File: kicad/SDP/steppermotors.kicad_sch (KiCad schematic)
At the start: 54 parts, among them J17 Conn_01x04, J18 Conn_01x04, J19 Conn_01x04, J20 Conn_01x04, J21 Conn_01x04, J22 Conn_01x04

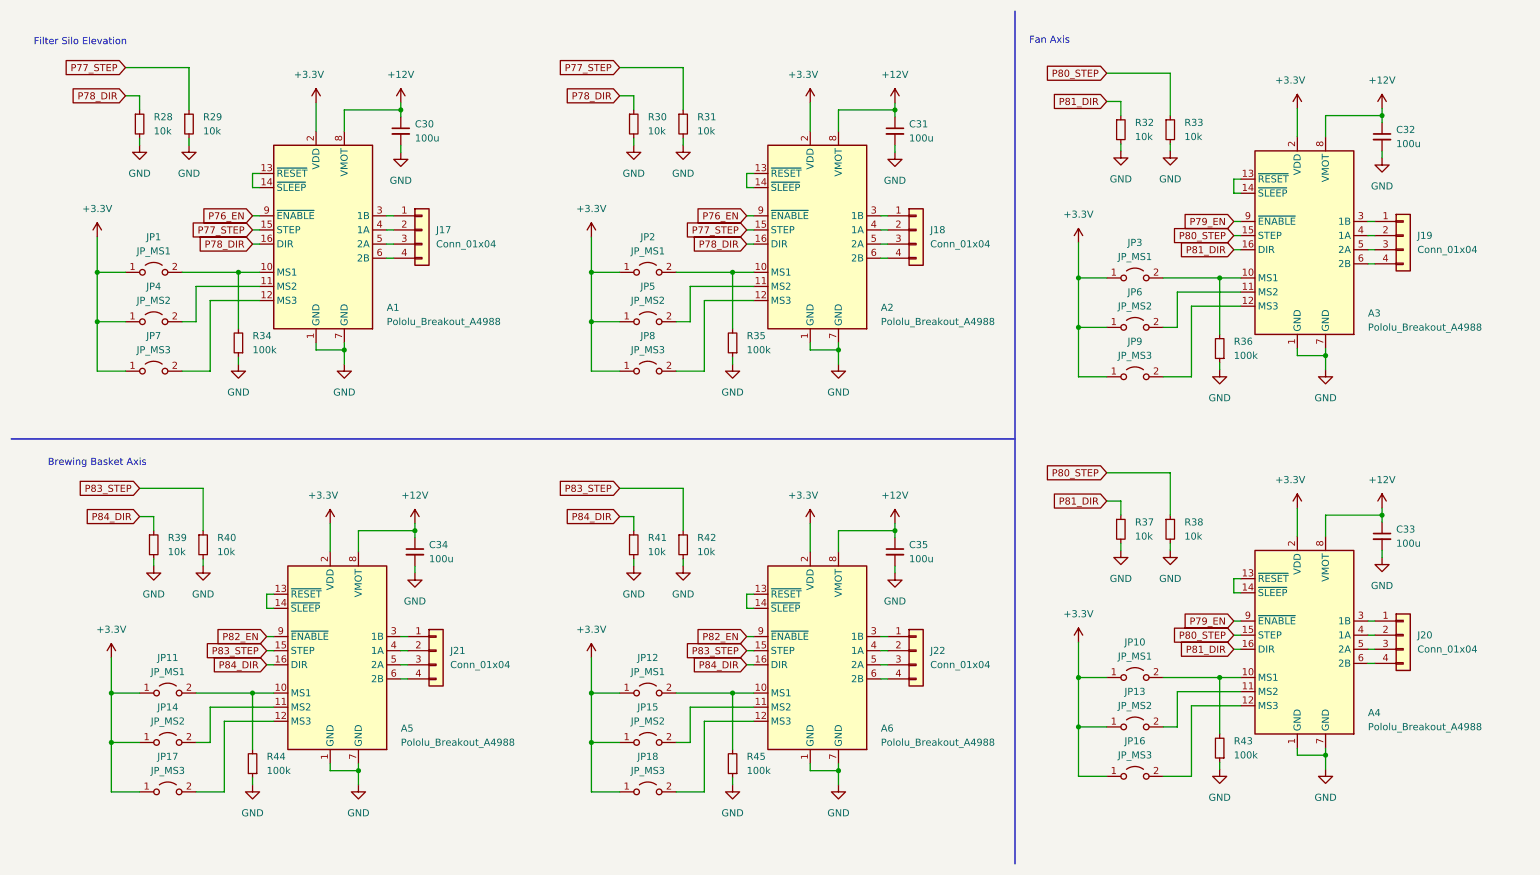
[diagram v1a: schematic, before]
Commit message: PCB layout and footprint assignment fix
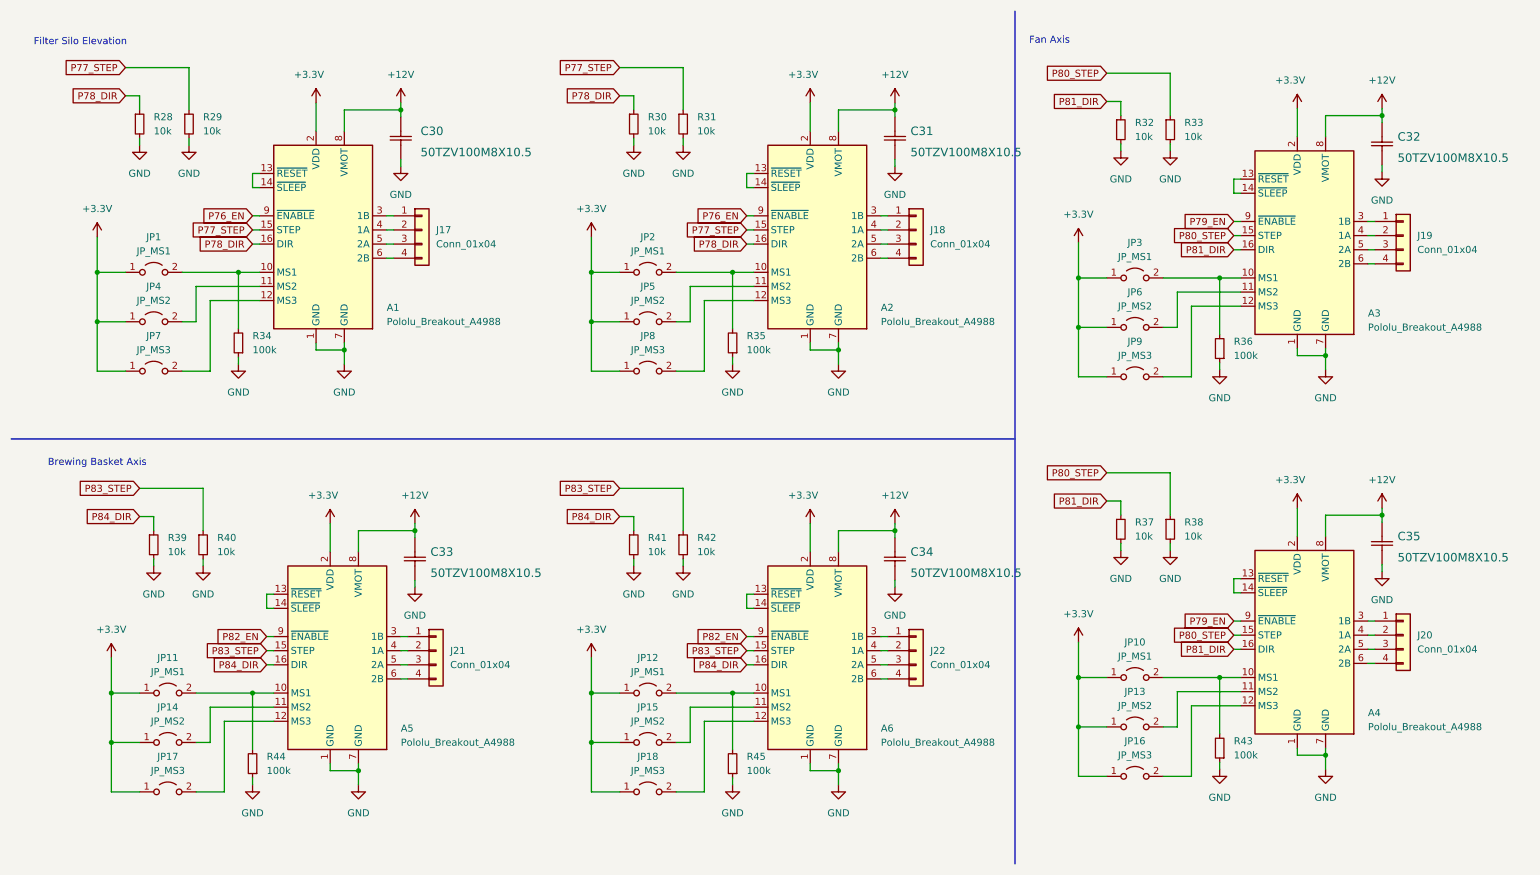
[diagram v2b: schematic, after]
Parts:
- removed C30, C31, C32, C33, C34, C35: 100u, footprints:50TZV100M8X10.5, symbol Device:C_Small
- added C30, C31, C32, C33, C34, C35: 50TZV100M8X10.5, 50TZV100M:50TZV100M8X10.5, symbol 2022-02-09_01-18-55:50TZV100M8X10.5
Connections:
- net +12V: now also C30.2, C31.2, C32.2, C33.2, C34.2, C35.2
- net GND: now also C30.1, C31.1, C32.1, C33.1, C34.1, C35.1
